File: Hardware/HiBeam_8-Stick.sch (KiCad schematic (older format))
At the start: 18 parts, among them J1 CONN_041X04_NO_SILK, J2 CONN_041X04_NO_SILK, U1 APA102, U2 APA102, U3 APA102, U4 APA102, U5 APA102, U6 APA102, U7 APA102, U8 APA102

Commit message: Fixed silk.
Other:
- note added: "HiBeams 8-Stick"
- note removed: "HiBeam 8-Stick"
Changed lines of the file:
@@
 5/31/17
 Text Notes 7350 7500 0    60   ~ 0
-HiBeam 8-Stick
+HiBeams 8-Stick
 $Comp
 L +5V #PWR12

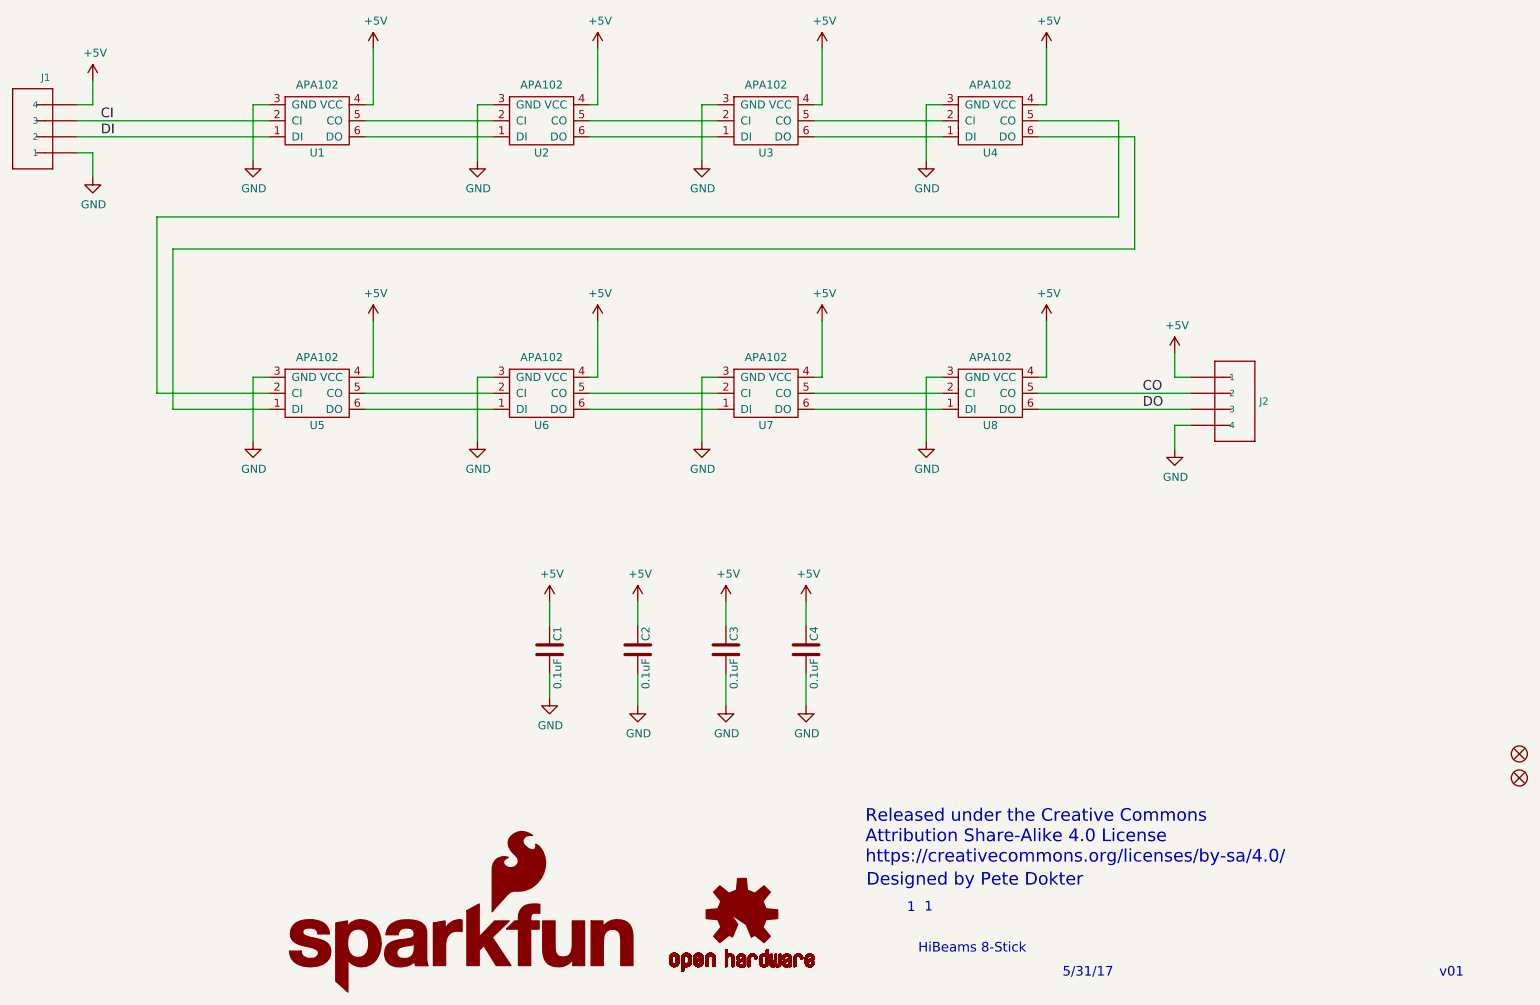
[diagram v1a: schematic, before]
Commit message: Added solder jumpers on the output lines.
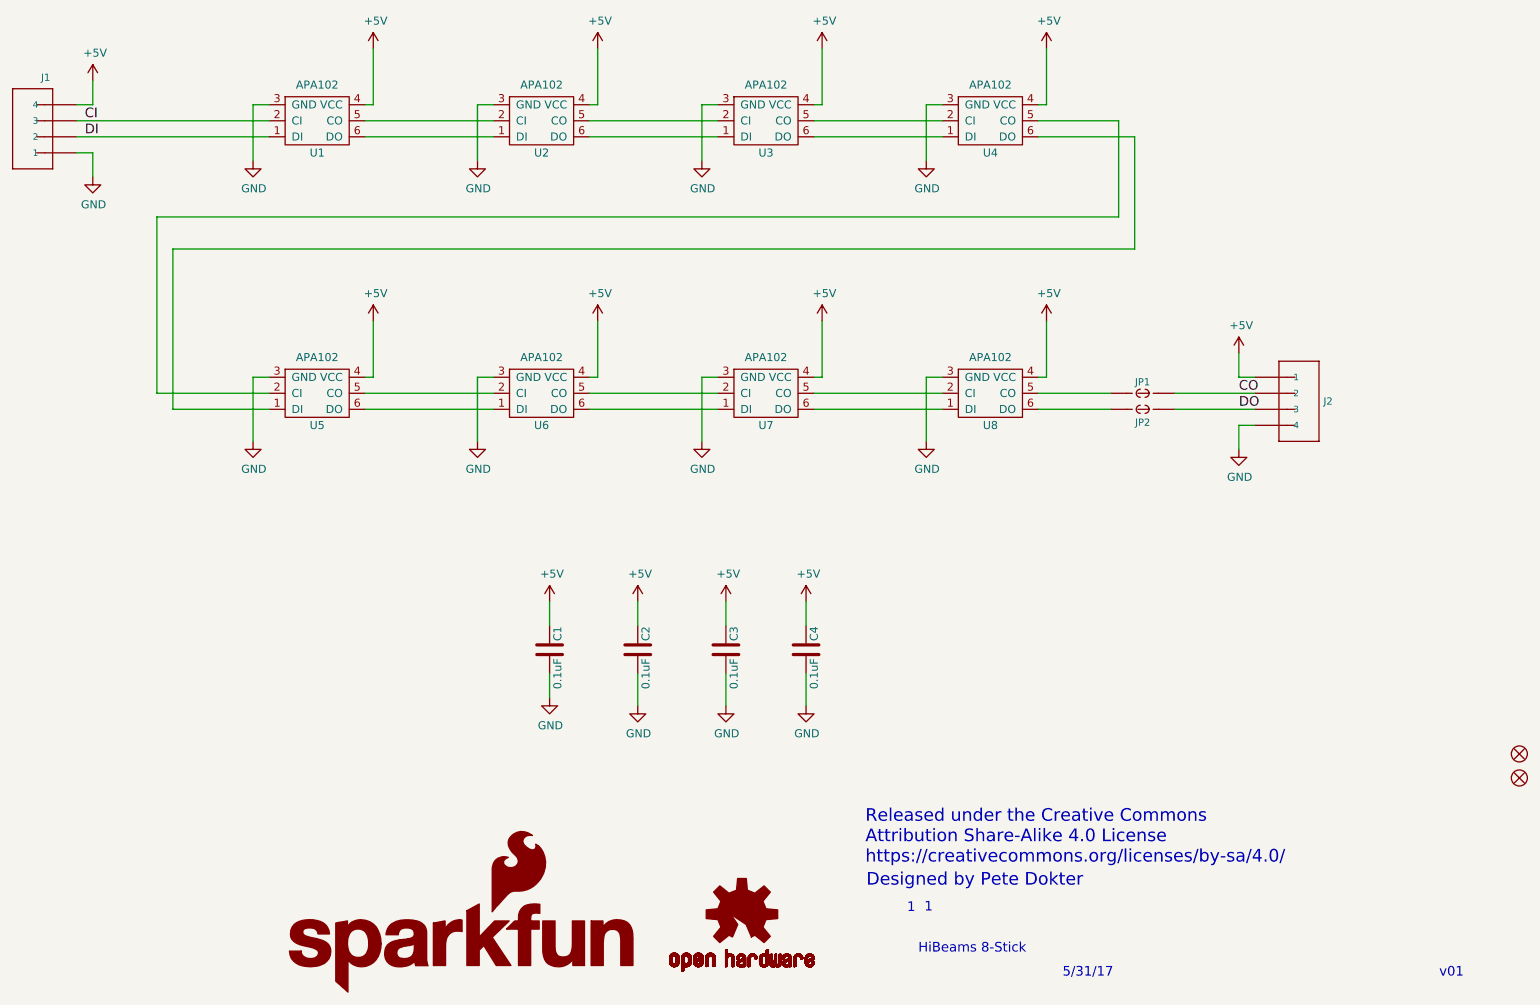
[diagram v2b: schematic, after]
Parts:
- added JP1, JP2: JUMPER-SMT_2_NC_TRACE_SILK, Jumpers:SMT-JUMPER_2_NC_TRACE_SILK, symbol JUMPER-SMT_2_NC_TRACE_SILK
- FD1, FD2: footprint FIDUCIAL-1X2 -> (none)
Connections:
- net CO: now also JP1.2; no longer U8.5 (CO)
- net DO: now also JP2.2; no longer U8.6 (DO)
- new net: JP1.1, U8.5 (CO)
- new net: JP2.1, U8.6 (DO)
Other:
- moved on the sheet: J2
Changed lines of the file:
@@
 $EndComp
 $Comp
-L +5V #PWR5
+L +5V #PWR01
 U 1 1 59134A1C
 P 3950 1850
-F 0 "#PWR5" H 3950 1700 50  0001 C CNN
+F 0 "#PWR01" H 3950 1700 50  0001 C CNN
 F 1 "+5V" H 3965 2023 50  0000 C CNN
 F 2 "" H 3950 1850 50  0001 C CNN
@@
 $EndComp
 $Comp
-L GND #PWR23
+L GND #PWR02
 U 1 1 59134AA5
 P 7400 2550
-F 0 "#PWR23" H 7400 2300 50  0001 C CNN
+F 0 "#PWR02" H 7400 2300 50  0001 C CNN
 F 1 "GND" H 7405 2377 50  0000 C CNN
 F 2 "" H 7400 2550 50  0001 C CNN
@@
 $EndComp
 $Comp
-L GND #PWR24
+L GND #PWR03
 U 1 1 59134AF7
 P 7400 4300
-F 0 "#PWR24" H 7400 4050 50  0001 C CNN
+F 0 "#PWR03" H 7400 4050 50  0001 C CNN
 F 1 "GND" H 7405 4127 50  0000 C CNN
 F 2 "" H 7400 4300 50  0001 C CNN
@@
 $EndComp
 $Comp
-L +5V #PWR6
+L +5V #PWR04
 U 1 1 59137399
 P 3950 3550
-F 0 "#PWR6" H 3950 3400 50  0001 C CNN
+F 0 "#PWR04" H 3950 3400 50  0001 C CNN
 F 1 "+5V" H 3965 3723 50  0000 C CNN
 F 2 "" H 3950 3550 50  0001 C CNN
@@
 $EndComp
 $Comp
-L +5V #PWR1
+L +5V #PWR05
 U 1 1 591374EE
 P 2200 2050
-F 0 "#PWR1" H 2200 1900 50  0001 C CNN
+F 0 "#PWR05" H 2200 1900 50  0001 C CNN
 F 1 "+5V" H 2215 2223 50  0000 C CNN
 F 2 "" H 2200 2050 50  0001 C CNN
@@
 $EndComp
 $Comp
-L GND #PWR2
+L GND #PWR06
 U 1 1 591375EB
 P 2200 2650
-F 0 "#PWR2" H 2200 2400 50  0001 C CNN
+F 0 "#PWR06" H 2200 2400 50  0001 C CNN
 F 1 "GND" H 2205 2477 50  0000 C CNN
 F 2 "" H 2200 2650 50  0001 C CNN
@@
 HiBeams 8-Stick
 $Comp
-L +5V #PWR12
+L +5V #PWR07
 U 1 1 591A0A66
 P 5350 3550
-F 0 "#PWR12" H 5350 3400 50  0001 C CNN
+F 0 "#PWR07" H 5350 3400 50  0001 C CNN
 F 1 "+5V" H 5365 3723 50  0000 C CNN
 F 2 "" H 5350 3550 50  0001 C CNN
@@
 $EndComp
 $Comp
-L +5V #PWR26
+L +5V #PWR08
 U 1 1 591A0A9D
 P 8150 3550
-F 0 "#PWR26" H 8150 3400 50  0001 C CNN
+F 0 "#PWR08" H 8150 3400 50  0001 C CNN
 F 1 "+5V" H 8165 3723 50  0000 C CNN
 F 2 "" H 8150 3550 50  0001 C CNN
@@
 $EndComp
 $Comp
-L +5V #PWR22
+L +5V #PWR09
 U 1 1 591A0BF2
 P 6750 3550
-F 0 "#PWR22" H 6750 3400 50  0001 C CNN
+F 0 "#PWR09" H 6750 3400 50  0001 C CNN
 F 1 "+5V" H 6765 3723 50  0000 C CNN
 F 2 "" H 6750 3550 50  0001 C CNN
@@
 $EndComp
 $Comp
-L GND #PWR16
+L GND #PWR010
 U 1 1 591A0CC3
 P 6000 4300
-F 0 "#PWR16" H 6000 4050 50  0001 C CNN
+F 0 "#PWR010" H 6000 4050 50  0001 C CNN
 F 1 "GND" H 6005 4127 50  0000 C CNN
 F 2 "" H 6000 4300 50  0001 C CNN
@@
 $EndComp
 $Comp
-L GND #PWR8
+L GND #PWR011
 U 1 1 591A0CFA
 P 4600 4300
-F 0 "#PWR8" H 4600 4050 50  0001 C CNN
+F 0 "#PWR011" H 4600 4050 50  0001 C CNN
 F 1 "GND" H 4605 4127 50  0000 C CNN
 F 2 "" H 4600 4300 50  0001 C CNN
@@
 $EndComp
 $Comp
-L GND #PWR4
+L GND #PWR012
 U 1 1 591A0DE1
 P 3200 4300
-F 0 "#PWR4" H 3200 4050 50  0001 C CNN
+F 0 "#PWR012" H 3200 4050 50  0001 C CNN
 F 1 "GND" H 3205 4127 50  0000 C CNN
 F 2 "" H 3200 4300 50  0001 C CNN
@@
 $EndComp
 $Comp
-L +5V #PWR11
+L +5V #PWR013
 U 1 1 591A34CC
 P 5350 1850
-F 0 "#PWR11" H 5350 1700 50  0001 C CNN
+F 0 "#PWR013" H 5350 1700 50  0001 C CNN
 F 1 "+5V" H 5365 2023 50  0000 C CNN
 F 2 "" H 5350 1850 50  0001 C CNN
@@
 $EndComp
 $Comp
-L +5V #PWR21
+L +5V #PWR014
 U 1 1 591A3503
 P 6750 1850
-F 0 "#PWR21" H 6750 1700 50  0001 C CNN
+F 0 "#PWR014" H 6750 1700 50  0001 C CNN
 F 1 "+5V" H 6765 2023 50  0000 C CNN
 F 2 "" H 6750 1850 50  0001 C CNN
@@
 $EndComp
 $Comp
-L +5V #PWR25
+L +5V #PWR015
 U 1 1 591A353A
 P 8150 1850
-F 0 "#PWR25" H 8150 1700 50  0001 C CNN
+F 0 "#PWR015" H 8150 1700 50  0001 C CNN
 F 1 "+5V" H 8165 2023 50  0000 C CNN
 F 2 "" H 8150 1850 50  0001 C CNN
@@
 $EndComp
 $Comp
-L GND #PWR15
+L GND #PWR016
 U 1 1 591A36BB
 P 6000 2550
-F 0 "#PWR15" H 6000 2300 50  0001 C CNN
+F 0 "#PWR016" H 6000 2300 50  0001 C CNN
 F 1 "GND" H 6005 2377 50  0000 C CNN
 F 2 "" H 6000 2550 50  0001 C CNN
@@
 $EndComp
 $Comp
-L GND #PWR7
+L GND #PWR017
 U 1 1 591A36F2
 P 4600 2550
-F 0 "#PWR7" H 4600 2300 50  0001 C CNN
+F 0 "#PWR017" H 4600 2300 50  0001 C CNN
 F 1 "GND" H 4605 2377 50  0000 C CNN
 F 2 "" H 4600 2550 50  0001 C CNN
@@
 $EndComp
 $Comp
-L GND #PWR3
+L GND #PWR018
 U 1 1 591A3729
 P 3200 2550
-F 0 "#PWR3" H 3200 2300 50  0001 C CNN
+F 0 "#PWR018" H 3200 2300 50  0001 C CNN
 F 1 "GND" H 3205 2377 50  0000 C CNN
 F 2 "" H 3200 2550 50  0001 C CNN
@@
 	2700 3100 2700 4100
 Wire Wire Line
-	8100 4000 9050 4000
-Wire Wire Line
-	8100 4100 9050 4100
-Wire Wire Line
 	7400 4300 7400 3900
 Wire Wire Line
@@
 	8150 3550 8150 3900
 $Comp
-L GND #PWR10
+L GND #PWR019
 U 1 1 592F86ED
 P 5050 5900
-F 0 "#PWR10" H 5050 5650 50  0001 C CNN
+F 0 "#PWR019" H 5050 5650 50  0001 C CNN
 F 1 "GND" H 5055 5727 50  0000 C CNN
 F 2 "" H 5050 5900 50  0001 C CNN
@@
 $EndComp
 $Comp
-L GND #PWR14
+L GND #PWR020
 U 1 1 592F8720
 P 5600 5950
-F 0 "#PWR14" H 5600 5700 50  0001 C CNN
+F 0 "#PWR020" H 5600 5700 50  0001 C CNN
 F 1 "GND" H 5605 5777 50  0000 C CNN
 F 2 "" H 5600 5950 50  0001 C CNN
@@
 $EndComp
 $Comp
-L GND #PWR18
+L GND #PWR021
 U 1 1 592F8753
 P 6150 5950
-F 0 "#PWR18" H 6150 5700 50  0001 C CNN
+F 0 "#PWR021" H 6150 5700 50  0001 C CNN
 F 1 "GND" H 6155 5777 50  0000 C CNN
 F 2 "" H 6150 5950 50  0001 C CNN
@@
 $EndComp
 $Comp
-L GND #PWR20
+L GND #PWR022
 U 1 1 592F8786
 P 6650 5950
-F 0 "#PWR20" H 6650 5700 50  0001 C CNN
+F 0 "#PWR022" H 6650 5700 50  0001 C CNN
 F 1 "GND" H 6655 5777 50  0000 C CNN
 F 2 "" H 6650 5950 50  0001 C CNN
@@
 $EndComp
 $Comp
-L +5V #PWR9
+L +5V #PWR023
 U 1 1 592F8895
 P 5050 5300
-F 0 "#PWR9" H 5050 5150 50  0001 C CNN
+F 0 "#PWR023" H 5050 5150 50  0001 C CNN
 F 1 "+5V" H 5065 5473 50  0000 C CNN
 F 2 "" H 5050 5300 50  0001 C CNN
@@
 $EndComp
 $Comp
-L +5V #PWR13
+L +5V #PWR024
 U 1 1 592F897C
 P 5600 5300
-F 0 "#PWR13" H 5600 5150 50  0001 C CNN
+F 0 "#PWR024" H 5600 5150 50  0001 C CNN
 F 1 "+5V" H 5615 5473 50  0000 C CNN
 F 2 "" H 5600 5300 50  0001 C CNN
@@
 $EndComp
 $Comp
-L +5V #PWR17
+L +5V #PWR025
 U 1 1 592F89AF
 P 6150 5300
-F 0 "#PWR17" H 6150 5150 50  0001 C CNN
+F 0 "#PWR025" H 6150 5150 50  0001 C CNN
 F 1 "+5V" H 6165 5473 50  0000 C CNN
 F 2 "" H 6150 5300 50  0001 C CNN
@@
 $EndComp
 $Comp
-L +5V #PWR19
+L +5V #PWR026
 U 1 1 592F8AAA
 P 6650 5300
-F 0 "#PWR19" H 6650 5150 50  0001 C CNN
+F 0 "#PWR026" H 6650 5150 50  0001 C CNN
 F 1 "+5V" H 6665 5473 50  0000 C CNN
 F 2 "" H 6650 5300 50  0001 C CNN
@@
 L CONN_041X04_NO_SILK J2
 U 1 1 592F92AC
-P 9250 4000
-F 0 "J2" H 9022 4050 45  0000 R CNN
-F 1 "CONN_041X04_NO_SILK" H 9023 4039 45  0001 R CNN
-F 2 "SFE_Connectors:1X04_NO_SILK" H 9280 4150 20  0001 C CNN
-F 3 "" H 9022 4092 60  0000 R CNN
-	1    9250 4000
+P 9650 4000
+F 0 "J2" H 9422 4050 45  0000 R CNN
+F 1 "CONN_041X04_NO_SILK" H 9423 4039 45  0001 R CNN
+F 2 "SFE_Connectors:1X04_NO_SILK" H 9680 4150 20  0001 C CNN
+F 3 "" H 9422 4092 60  0000 R CNN
+	1    9650 4000
 	-1   0    0    1
 $EndComp
@@
 	2200 2500 2200 2650
 $Comp
-L +5V #PWR27
+L +5V #PWR027
 U 1 1 592F9E01
-P 8950 3750
-F 0 "#PWR27" H 8950 3600 50  0001 C CNN
-F 1 "+5V" H 8965 3923 50  0000 C CNN
-F 2 "" H 8950 3750 50  0001 C CNN
-F 3 "" H 8950 3750 50  0001 C CNN
-	1    8950 3750
-	1    0    0    -1
-$EndComp
-$Comp
-L GND #PWR28
+P 9350 3750
+F 0 "#PWR027" H 9350 3600 50  0001 C CNN
+F 1 "+5V" H 9365 3923 50  0000 C CNN
+F 2 "" H 9350 3750 50  0001 C CNN
+F 3 "" H 9350 3750 50  0001 C CNN
+	1    9350 3750
+	1    0    0    -1
+$EndComp
+$Comp
+L GND #PWR028
 U 1 1 592F9E60
-P 8950 4350
-F 0 "#PWR28" H 8950 4100 50  0001 C CNN
-F 1 "GND" H 8955 4177 50  0000 C CNN
-F 2 "" H 8950 4350 50  0001 C CNN
-F 3 "" H 8950 4350 50  0001 C CNN
-	1    8950 4350
-	1    0    0    -1
-$EndComp
-Wire Wire Line
-	8950 3750 8950 3900
-Wire Wire Line
-	8950 3900 9050 3900
-Wire Wire Line
-	9050 4200 8950 4200
-Wire Wire Line
-	8950 4200 8950 4350
+P 9350 4350
+F 0 "#PWR028" H 9350 4100 50  0001 C CNN
+F 1 "GND" H 9355 4177 50  0000 C CNN
+F 2 "" H 9350 4350 50  0001 C CNN
+F 3 "" H 9350 4350 50  0001 C CNN
+	1    9350 4350
+	1    0    0    -1
+$EndComp
+Wire Wire Line
+	9350 3750 9350 3900
+Wire Wire Line
+	9350 3900 9450 3900
+Wire Wire Line
+	9450 4200 9350 4200
+Wire Wire Line
+	9350 4200 9350 4350
 Wire Wire Line
 	2100 2300 3300 2300
 Wire Wire Line
 	2100 2400 3300 2400
-Text Label 2250 2300 0    60   ~ 0
+Text Label 2150 2300 0    60   ~ 0
 CI
-Text Label 2250 2400 0    60   ~ 0
+Text Label 2150 2400 0    60   ~ 0
 DI
-Text Label 8750 4000 0    60   ~ 0
+Text Label 9350 4000 0    60   ~ 0
 CO
-Text Label 8750 4100 0    60   ~ 0
+Text Label 9350 4100 0    60   ~ 0
 DO
 $Comp
@@
 F 0 "FD2" H 11100 6400 45  0001 C CNN
 F 1 "FIDUCIAL1X2" H 11100 6400 45  0001 C CNN
-F 2 "FIDUCIAL-1X2" H 11130 6550 20  0001 C CNN
+F 2 "" H 11130 6550 20  0001 C CNN
 F 3 "XXX-00000" H 11178 6400 60  0001 L CNN
 	1    11100 6400
@@
 F 0 "FD1" H 11100 6250 45  0001 C CNN
 F 1 "FIDUCIAL1X2" H 11100 6250 45  0001 C CNN
-F 2 "FIDUCIAL-1X2" H 11130 6400 20  0001 C CNN
+F 2 "" H 11130 6400 20  0001 C CNN
 F 3 "XXX-00000" H 11178 6250 60  0001 L CNN
 	1    11100 6250
 	1    0    0    -1
 $EndComp
+$Comp
+L JUMPER-SMT_2_NC_TRACE_SILK JP1
+U 1 1 595FB3A1
+P 8750 4000
+F 0 "JP1" H 8749 4070 45  0000 C CNN
+F 1 "JUMPER-SMT_2_NC_TRACE_SILK" H 8750 4201 45  0001 C CNN
+F 2 "Jumpers:SMT-JUMPER_2_NC_TRACE_SILK" H 8780 4150 20  0001 C CNN
+F 3 "XXX-00000" H 8750 4106 60  0001 C CNN
+	1    8750 4000
+	1    0    0    -1
+$EndComp
+$Comp
+L JUMPER-SMT_2_NC_TRACE_SILK JP2
+U 1 1 595FB493
+P 8750 4100
+F 0 "JP2" H 8750 4018 45  0000 C CNN
+F 1 "JUMPER-SMT_2_NC_TRACE_SILK" H 8750 4301 45  0001 C CNN
+F 2 "Jumpers:SMT-JUMPER_2_NC_TRACE_SILK" H 8780 4250 20  0001 C CNN
+F 3 "XXX-00000" H 8750 4206 60  0001 C CNN
+	1    8750 4100
+	1    0    0    -1
+$EndComp
+Wire Wire Line
+	8550 4000 8100 4000
+Wire Wire Line
+	8100 4100 8550 4100
+Wire Wire Line
+	8950 4000 9450 4000
+Wire Wire Line
+	9450 4100 8950 4100
 $EndSCHEMATC
